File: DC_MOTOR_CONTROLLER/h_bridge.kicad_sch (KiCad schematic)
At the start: 1 part, among them U3 L298HN

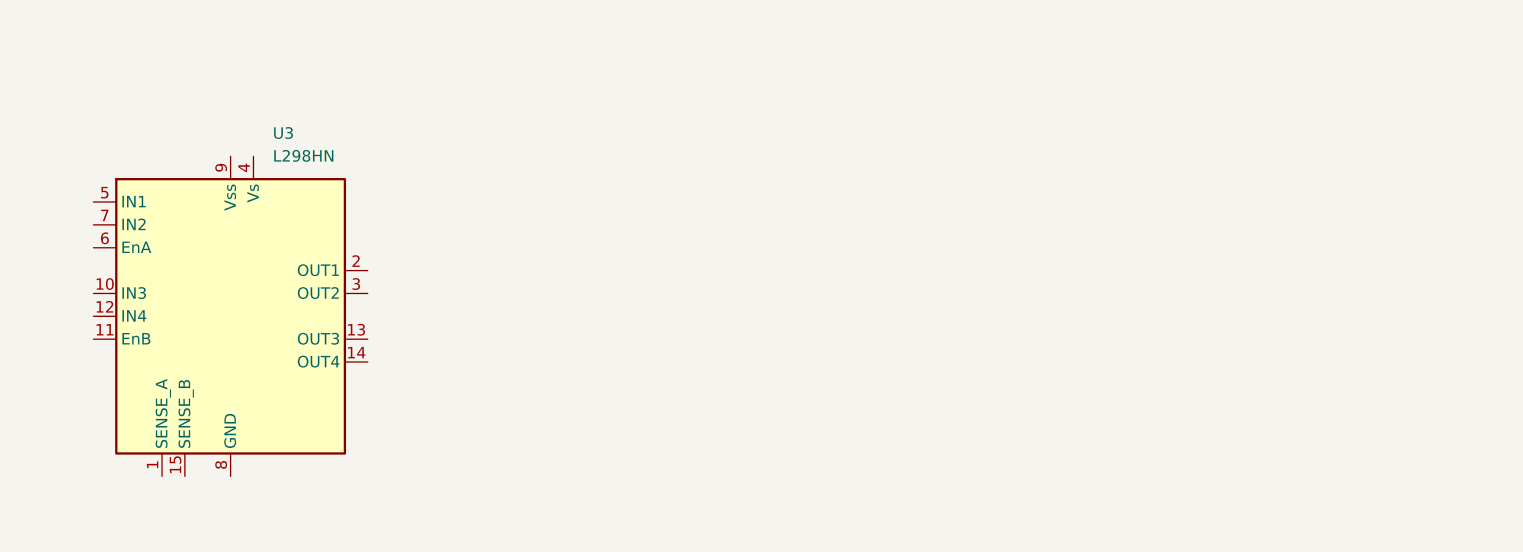
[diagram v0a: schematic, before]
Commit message: worked on h-bridge, pwm, io
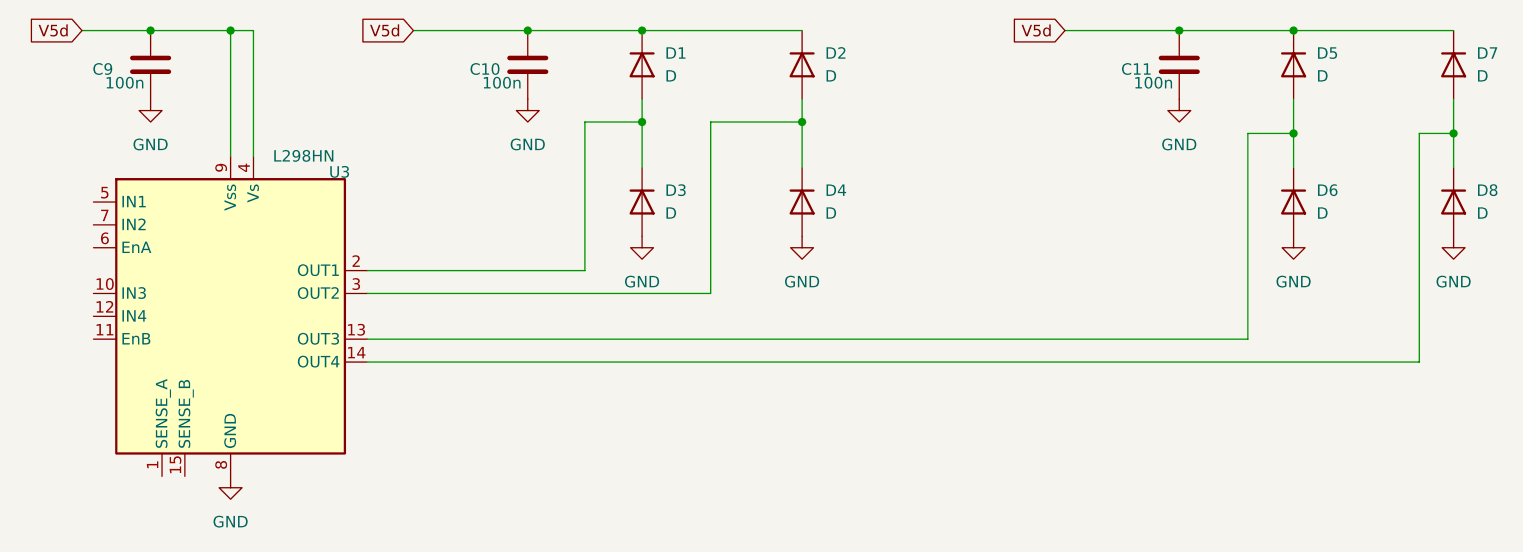
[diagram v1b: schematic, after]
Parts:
- added C10, C11, C9: 100n, symbol Device:C
- added D1, D2, D3, D4, D5, D6, D7, D8: D, symbol Device:D
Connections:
- net at U3.13 (OUT3): now also D5.2 (A), D6.1 (K)
- net at U3.14 (OUT4): now also D7.2 (A), D8.1 (K)
- net at U3.2 (OUT1): now also D1.2 (A), D3.1 (K)
- net at U3.3 (OUT2): now also D2.2 (A), D4.1 (K)
- net V5d: now reaches U3.4 (Vs)
- net V5d: now also U3.9 (Vss), C10.1, C11.1, C9.1, D1.1 (K), D2.1 (K), D5.1 (K), D7.1 (K)
- net GND: now reaches U3.8 (GND)
- net GND: now also C10.2, C11.2, C9.2, D3.2 (A), D4.2 (A), D6.2 (A), D8.2 (A)
